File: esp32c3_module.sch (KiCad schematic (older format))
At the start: 13 parts, among them J1 Conn_01x15_Male, J2 Conn_01x15_Male, SW1 BOOT, SW2 RST, U3 ESP32-C3-MINI-1

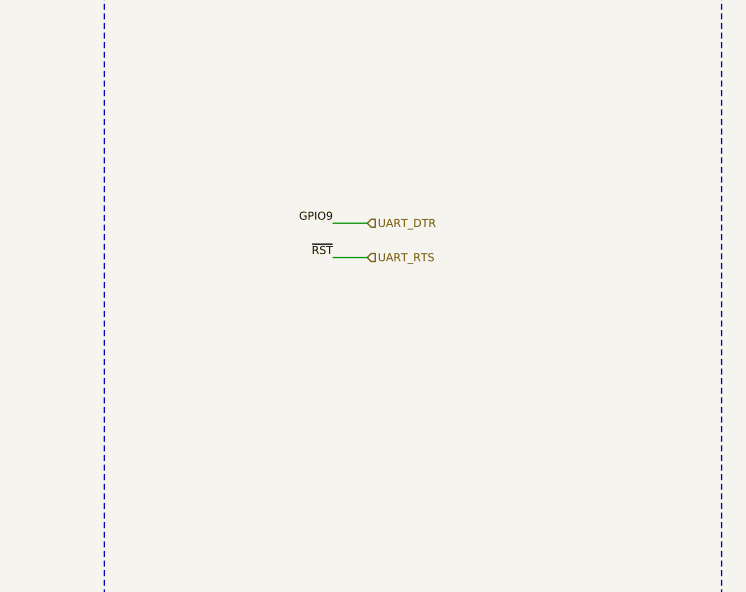
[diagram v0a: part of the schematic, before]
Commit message: Replace CP2102 with CH340X
Also add BJTs to ESP32C3 strapping pins
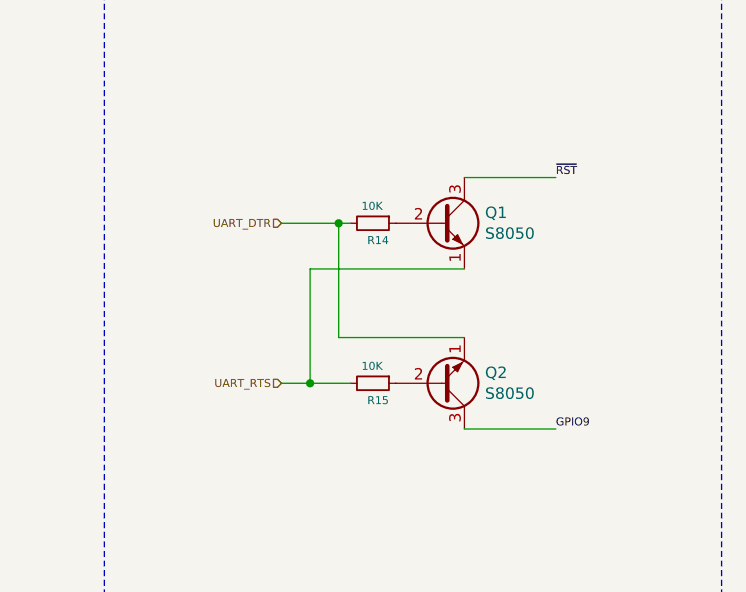
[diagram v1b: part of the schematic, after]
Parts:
- added Q1, Q2: S8050, Package_TO_SOT_SMD:SOT-23, symbol Transistor_BJT:S8050
- added R14, R15: 10K, Resistor_SMD:R_0402_1005Metric, symbol Device:R_Small
- SW1, SW2: footprint Button_Switch_SMD:SW_SPST_TL3342 -> Button_Switch_SMD:SW_SPST_CK_RS282G05A3
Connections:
- wire segments 63 -> 71
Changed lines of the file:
@@
 F 0 "SW2" H 1500 6550 35  0000 C CNN
 F 1 "RST" H 1500 6350 35  0000 C CNN
-F 2 "Button_Switch_SMD:SW_SPST_TL3342" H 1500 6600 50  0001 C CNN
+F 2 "Button_Switch_SMD:SW_SPST_CK_RS282G05A3" H 1500 6600 50  0001 C CNN
 F 3 "https://datasheet.lcsc.com/lcsc/2002271431_XKB-Connectivity-TS-1187A-B-A-B_C318884.pdf" H 1500 6600 50  0001 C CNN
 F 4 "C318884" H 1500 6400 50  0001 C CNN "LCSC"
@@
 F 0 "SW1" H 1500 6050 35  0000 C CNN
 F 1 "BOOT" H 1500 5850 35  0000 C CNN
-F 2 "Button_Switch_SMD:SW_SPST_TL3342" H 1500 6100 50  0001 C CNN
+F 2 "Button_Switch_SMD:SW_SPST_CK_RS282G05A3" H 1500 6100 50  0001 C CNN
 F 3 "https://datasheet.lcsc.com/lcsc/2002271431_XKB-Connectivity-TS-1187A-B-A-B_C318884.pdf" H 1500 6100 50  0001 C CNN
 F 4 "C318884" H 1500 5900 50  0001 C CNN "LCSC"
@@
 Text HLabel 7550 2100 0    35   Input ~ 0
 UART_RXD
-Wire Wire Line
-	9650 2300 9500 2300
-Wire Wire Line
-	9650 2450 9500 2450
-Text HLabel 9650 2300 2    35   Input ~ 0
+Text HLabel 9275 2300 0    35   Input ~ 0
 UART_DTR
-Text HLabel 9650 2450 2    35   Input ~ 0
+Text HLabel 9275 3000 0    35   Input ~ 0
 UART_RTS
 Text Label 1800 5900 0    35   ~ 0
 GPIO9
-Text Label 9500 2300 2    35   ~ 0
+Text Label 10475 3200 0    35   ~ 0
 GPIO9
 Text Label 1650 3050 2    35   ~ 0
@@
 Text Label 1150 2950 2    35   ~ 0
 GPIO8
-Text Label 9500 2450 2    35   ~ 0
+Text Label 10475 2100 0    35   ~ 0
 ~RST
 Text Label 1350 1250 2    35   ~ 0
@@
 Wire Notes Line
 	2500 4700 2500 7750
+$Comp
+L Transistor_BJT:S8050 Q1
+U 1 1 63DDD419
+P 9975 2300
+F 0 "Q1" H 10165 2346 50  0000 L CNN
+F 1 "S8050" H 10165 2255 50  0000 L CNN
+F 2 "Package_TO_SOT_SMD:SOT-23" H 10175 2225 50  0001 L CIN
+F 3 "http://www.unisonic.com.tw/datasheet/S8050.pdf" H 9975 2300 50  0001 L CNN
+F 4 "C2146" H 9975 2300 50  0001 C CNN "LCSC"
+	1    9975 2300
+	1    0    0    -1
+$EndComp
+$Comp
+L Transistor_BJT:S8050 Q2
+U 1 1 63DDD9FC
+P 9975 3000
+F 0 "Q2" H 10165 2954 50  0000 L CNN
+F 1 "S8050" H 10165 3045 50  0000 L CNN
+F 2 "Package_TO_SOT_SMD:SOT-23" H 10175 2925 50  0001 L CIN
+F 3 "http://www.unisonic.com.tw/datasheet/S8050.pdf" H 9975 3000 50  0001 L CNN
+F 4 "C2146" H 9975 3000 50  0001 C CNN "LCSC"
+	1    9975 3000
+	1    0    0    1
+$EndComp
+$Comp
+L Device:R_Small R?
+U 1 1 63DE663C
+P 9675 3000
+AR Path="/63DE663C" Ref="R?"  Part="1"
+AR Path="/63833C0B/63DE663C" Ref="R15"  Part="1"
+F 0 "R15" V 9750 2975 35  0000 L CNN
+F 1 "10K" V 9600 2950 35  0000 L CNN
+F 2 "Resistor_SMD:R_0402_1005Metric" H 9675 3000 50  0001 C CNN
+F 3 "https://datasheet.lcsc.com/lcsc/2206010100_UNI-ROYAL-Uniroyal-Elec-0402WGF1002TCE_C25744.pdf" H 9675 3000 50  0001 C CNN
+F 4 "C25744" H 9675 3000 50  0001 C CNN "LCSC"
+	1    9675 3000
+	0    1    1    0
+$EndComp
+$Comp
+L Device:R_Small R?
+U 1 1 63DE8970
+P 9675 2300
+AR Path="/63DE8970" Ref="R?"  Part="1"
+AR Path="/63833C0B/63DE8970" Ref="R14"  Part="1"
+F 0 "R14" V 9750 2275 35  0000 L CNN
+F 1 "10K" V 9600 2250 35  0000 L CNN
+F 2 "Resistor_SMD:R_0402_1005Metric" H 9675 2300 50  0001 C CNN
+F 3 "https://datasheet.lcsc.com/lcsc/2206010100_UNI-ROYAL-Uniroyal-Elec-0402WGF1002TCE_C25744.pdf" H 9675 2300 50  0001 C CNN
+F 4 "C25744" H 9675 2300 50  0001 C CNN "LCSC"
+	1    9675 2300
+	0    1    1    0
+$EndComp
+Wire Wire Line
+	9525 2300 9525 2800
+Wire Wire Line
+	9525 2800 10075 2800
+Connection ~ 9525 2300
+Wire Wire Line
+	9525 2300 9575 2300
+Wire Wire Line
+	9275 2300 9525 2300
+Wire Wire Line
+	9275 3000 9400 3000
+Wire Wire Line
+	9400 2500 9400 3000
+Wire Wire Line
+	9400 2500 10075 2500
+Connection ~ 9400 3000
+Wire Wire Line
+	9400 3000 9575 3000
+Wire Wire Line
+	10075 3200 10475 3200
+Wire Wire Line
+	10075 2100 10475 2100
 $EndSCHEMATC

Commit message: Use ESP32-C3-WROOM-02 module
Signed-off-by: Tomislav Milkovic <tomislav.milkovic95@gmail.com>
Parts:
- removed D1: USR_LED, LED_SMD:LED_0603_1608Metric, symbol Device:LED_Small
- removed R19: 470Ω, Resistor_SMD:R_0603_1608Metric, symbol Device:R_Small
- removed U3: ESP32-C3-MINI-1, Espressif:ESP32-C3-MINI-1, symbol Espressif:ESP32-C3-MINI-1
- added D1: WS2812B, LED_SMD:LED_WS2812B_PLCC4_5.0x5.0mm_P3.2mm, symbol LED:WS2812B
- added U3: ESP32-C3-WROOM-02, Espressif:ESP32-C3-WROOM-02, symbol Espressif:ESP32-C3-WROOM-02
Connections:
- net labels added: ESP32_UART_DTR, ESP32_UART_RTS, ESP32_UART_RXD, ESP32_UART_TXD, ESP32_USB_D+, ESP32_USB_D-, GPIO18, GPIO19, GPIO20, GPIO21
- net labels removed: JTAG_USB_D+, JTAG_USB_D-, UART_DTR, UART_RTS, UART_RXD, UART_TXD, USR_LED_A
- wire segments 71 -> 66
- no-connect marks 14 -> 1
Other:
- note removed: "Blue LED"
- note removed: "~~1.8 mA LED current"
- moved on the sheet: R16, R17

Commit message: Change USB UART adapter to CP2102
Signed-off-by: Tomislav Milkovic <tomislav.milkovic95@gmail.com>
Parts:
- U3: footprint Espressif:ESP32-C3-WROOM-02 -> Espressif custom:ESP32-C3-WROOM-02-SOCKET
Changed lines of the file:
@@
 $Descr A4 11693 8268
 encoding utf-8
-Sheet 4 5
+Sheet 3 5
 Title "ESP32-C3 module"
 Date "2022-11-20"
@@
 F 0 "U3" H 2725 4115 50  0000 C CNN
 F 1 "ESP32-C3-WROOM-02" H 2725 4024 50  0000 C CNN
-F 2 "Espressif:ESP32-C3-WROOM-02" H 2700 1400 50  0001 C CNN
+F 2 "Espressif custom:ESP32-C3-WROOM-02-SOCKET" H 2700 1400 50  0001 C CNN
 F 3 "https://www.espressif.com/sites/default/files/documentation/esp32-c3-wroom-02_datasheet_en.pdf" H 250 1400 50  0001 C CNN
 	1    2700 2700

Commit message: Add LCSC part numbers for all components
Signed-off-by: Tomislav Milkovic <tomislav.milkovic95@gmail.com>
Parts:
- C17: LCSC C440198 -> C19702
- D1: value WS2812B -> WS2812C; footprint LED_SMD:LED_WS2812B_PLCC4_5.0x5.0mm_P3.2mm -> LED_custom:LED_WS2812B_2.0x2.0mm_P1.13mm; LCSC (none) -> C2976072
- SW1, SW2: LCSC C318884 -> (none)
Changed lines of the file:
@@
 Sheet 3 5
 Title "ESP32-C3 module"
-Date "2022-11-20"
+Date "2025-02-16"
 Rev "1.0"
 Comp "Copyright: Tomislav Milkovic"
@@
 F 2 "Button_Switch_SMD:SW_SPST_CK_RS282G05A3" H 1500 6600 50  0001 C CNN
 F 3 "https://datasheet.lcsc.com/lcsc/2002271431_XKB-Connectivity-TS-1187A-B-A-B_C318884.pdf" H 1500 6600 50  0001 C CNN
-F 4 "C318884" H 1500 6400 50  0001 C CNN "LCSC"
+F 4 "" H 1500 6400 50  0001 C CNN "LCSC"
 	1    1500 6400
 	1    0    0    -1
@@
 F 2 "Capacitor_SMD:C_0603_1608Metric" H 1200 3850 50  0001 C CNN
 F 3 "https://datasheet.lcsc.com/lcsc/2004251506_Murata-Electronics-GRM21BR61H106KE43L_C440198.pdf" H 1200 3850 50  0001 C CNN
-F 4 "C440198" H 1200 3850 50  0001 C CNN "LCSC"
+F 4 "C19702" H 1200 3850 50  0001 C CNN "LCSC"
 	1    1200 3850
 	1    0    0    -1
@@
 F 2 "Button_Switch_SMD:SW_SPST_CK_RS282G05A3" H 1500 6100 50  0001 C CNN
 F 3 "https://datasheet.lcsc.com/lcsc/2002271431_XKB-Connectivity-TS-1187A-B-A-B_C318884.pdf" H 1500 6100 50  0001 C CNN
-F 4 "C318884" H 1500 5900 50  0001 C CNN "LCSC"
+F 4 "" H 1500 5900 50  0001 C CNN "LCSC"
 	1    1500 5900
 	1    0    0    -1
@@
 	1    0    0    -1
 $EndComp
-Text Notes 4100 7750 0    47   ~ 9
+Text Notes 4450 7750 0    47   ~ 9
 User LED
 $Comp
@@
 F 2 "Connector_PinHeader_2.54mm:PinHeader_1x15_P2.54mm_Vertical" H 7750 2600 50  0001 C CNN
 F 3 "~" H 7750 2600 50  0001 C CNN
+F 4 "" H 7750 2600 50  0001 C CNN "LCSC"
 	1    7750 2600
 	1    0    0    -1
@@
 F 2 "Connector_PinHeader_2.54mm:PinHeader_1x15_P2.54mm_Vertical" H 6200 2600 50  0001 C CNN
 F 3 "~" H 6200 2600 50  0001 C CNN
+F 4 "" H 6200 2600 50  0001 C CNN "LCSC"
 	1    6200 2600
 	1    0    0    -1
@@
 F 1 "S8050" H 10165 2255 50  0000 L CNN
 F 2 "Package_TO_SOT_SMD:SOT-23" H 10175 2225 50  0001 L CIN
-F 3 "http://www.unisonic.com.tw/datasheet/S8050.pdf" H 9975 2300 50  0001 L CNN
+F 3 "https://www.lcsc.com/datasheet/lcsc_datasheet_2310131500_Jiangsu-Changjing-Electronics-Technology-Co---Ltd--S8050-J3Y-RANGE-200-350_C2146.pdf" H 9975 2300 50  0001 L CNN
 F 4 "C2146" H 9975 2300 50  0001 C CNN "LCSC"
 	1    9975 2300
@@
 F 1 "S8050" H 10165 3045 50  0000 L CNN
 F 2 "Package_TO_SOT_SMD:SOT-23" H 10175 2925 50  0001 L CIN
-F 3 "http://www.unisonic.com.tw/datasheet/S8050.pdf" H 9975 3000 50  0001 L CNN
+F 3 "https://www.lcsc.com/datasheet/lcsc_datasheet_2310131500_Jiangsu-Changjing-Electronics-Technology-Co---Ltd--S8050-J3Y-RANGE-200-350_C2146.pdf" H 9975 3000 50  0001 L CNN
 F 4 "C2146" H 9975 3000 50  0001 C CNN "LCSC"
 	1    9975 3000
@@
 F 2 "Espressif custom:ESP32-C3-WROOM-02-SOCKET" H 2700 1400 50  0001 C CNN
 F 3 "https://www.espressif.com/sites/default/files/documentation/esp32-c3-wroom-02_datasheet_en.pdf" H 250 1400 50  0001 C CNN
+F 4 "" H 2700 2700 50  0001 C CNN "LCSC"
 	1    2700 2700
 	1    0    0    -1
@@
 U 1 1 67B7102E
 P 3525 5950
-F 0 "D1" H 3675 6200 50  0000 L CNN
-F 1 "WS2812B" H 3600 5700 50  0000 L CNN
-F 2 "LED_SMD:LED_WS2812B_PLCC4_5.0x5.0mm_P3.2mm" H 3575 5650 50  0001 L TNN
-F 3 "https://cdn-shop.adafruit.com/datasheets/WS2812B.pdf" H 3625 5575 50  0001 L TNN
+F 0 "D1" H 3650 6200 50  0000 L CNN
+F 1 "WS2812C" H 3575 5700 50  0000 L CNN
+F 2 "LED_custom:LED_WS2812B_2.0x2.0mm_P1.13mm" H 3575 5650 50  0001 L TNN
+F 3 "https://wmsc.lcsc.com/wmsc/upload/file/pdf/v2/lcsc/2202221130_Worldsemi-WS2812C-2020-V1_C2976072.pdf" H 3625 5575 50  0001 L TNN
+F 4 "C2976072" H 3525 5950 50  0001 C CNN "LCSC"
 	1    3525 5950
 	1    0    0    -1

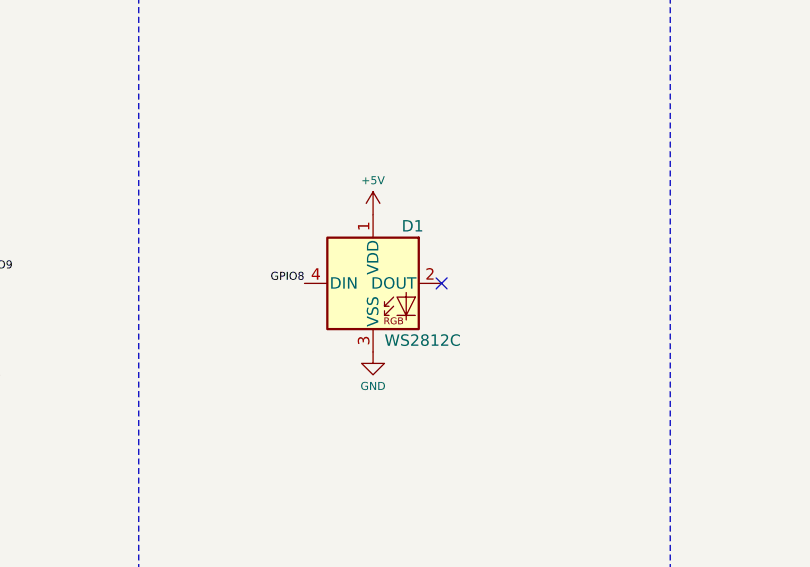
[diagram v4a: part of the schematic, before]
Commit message: Replace WS2812B with SK6805 RGB LED
Signed-off-by: Tomislav Milkovic <tomislav.milkovic95@gmail.com>
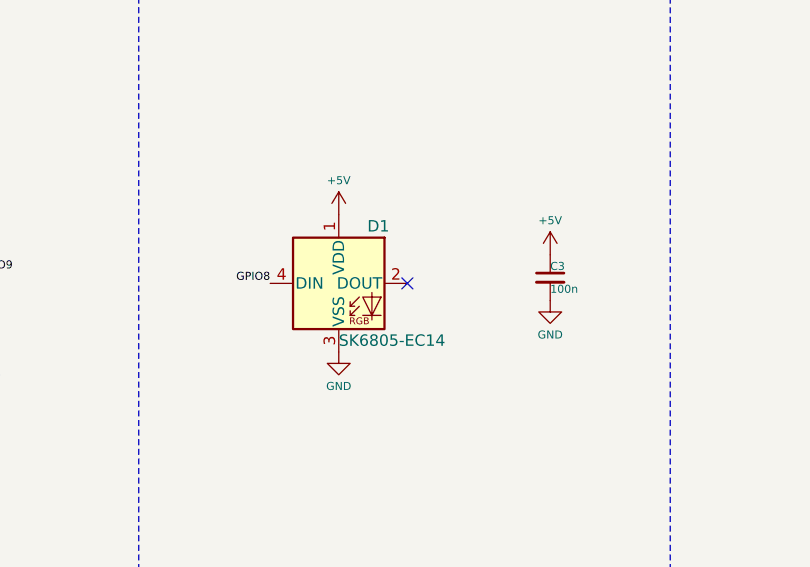
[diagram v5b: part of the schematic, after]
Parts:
- added C3: 100n, Capacitor_SMD:C_0402_1005Metric, symbol Device:C_Small
- D1: value WS2812C -> SK6805-EC14; footprint LED_custom:LED_WS2812B_2.0x2.0mm_P1.13mm -> LED_custom:LED_SK6805_E14_1.4x1.4mm_P0.4mm; LCSC C2976072 -> C2909055
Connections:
- net +5V: now also C3.1
- net GND: now also C3.2
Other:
- moved on the sheet: D1
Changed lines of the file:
@@
 L LED:WS2812B D1
 U 1 1 67B7102E
-P 3525 5950
-F 0 "D1" H 3650 6200 50  0000 L CNN
-F 1 "WS2812C" H 3575 5700 50  0000 L CNN
-F 2 "LED_custom:LED_WS2812B_2.0x2.0mm_P1.13mm" H 3575 5650 50  0001 L TNN
-F 3 "https://wmsc.lcsc.com/wmsc/upload/file/pdf/v2/lcsc/2202221130_Worldsemi-WS2812C-2020-V1_C2976072.pdf" H 3625 5575 50  0001 L TNN
-F 4 "C2976072" H 3525 5950 50  0001 C CNN "LCSC"
-	1    3525 5950
+P 3375 5950
+F 0 "D1" H 3500 6200 50  0000 L CNN
+F 1 "SK6805-EC14" H 3375 5700 50  0000 L CNN
+F 2 "LED_custom:LED_SK6805_E14_1.4x1.4mm_P0.4mm" H 3425 5650 50  0001 L TNN
+F 3 "https://wmsc.lcsc.com/wmsc/upload/file/pdf/v2/lcsc/2202161430_OPSCO-Optoelectronics-SK6805-EC14_C2909055.pdf" H 3475 5575 50  0001 L TNN
+F 4 "C2909055" H 3375 5950 50  0001 C CNN "LCSC"
+	1    3375 5950
 	1    0    0    -1
 $EndComp
@@
 L power:+5V #PWR?
 U 1 1 67B72448
-P 3525 5650
+P 3375 5650
 AR Path="/67B72448" Ref="#PWR?"  Part="1"
 AR Path="/63833C0B/67B72448" Ref="#PWR0104"  Part="1"
-F 0 "#PWR0104" H 3525 5500 50  0001 C CNN
-F 1 "+5V" H 3525 5800 35  0000 C CNN
-F 2 "" H 3525 5650 50  0001 C CNN
-F 3 "" H 3525 5650 50  0001 C CNN
-	1    3525 5650
+F 0 "#PWR0104" H 3375 5500 50  0001 C CNN
+F 1 "+5V" H 3375 5800 35  0000 C CNN
+F 2 "" H 3375 5650 50  0001 C CNN
+F 3 "" H 3375 5650 50  0001 C CNN
+	1    3375 5650
 	1    0    0    -1
 $EndComp
@@
 L power:GND #PWR?
 U 1 1 67B73827
-P 3525 6250
+P 3375 6250
 AR Path="/67B73827" Ref="#PWR?"  Part="1"
 AR Path="/63833C0B/67B73827" Ref="#PWR0105"  Part="1"
-F 0 "#PWR0105" H 3525 6000 50  0001 C CNN
-F 1 "GND" H 3525 6100 35  0000 C CNN
-F 2 "" H 3525 6250 50  0001 C CNN
-F 3 "" H 3525 6250 50  0001 C CNN
-	1    3525 6250
+F 0 "#PWR0105" H 3375 6000 50  0001 C CNN
+F 1 "GND" H 3375 6100 35  0000 C CNN
+F 2 "" H 3375 6250 50  0001 C CNN
+F 3 "" H 3375 6250 50  0001 C CNN
+	1    3375 6250
 	1    0    0    -1
 $EndComp
-Text Label 3225 5950 2    35   ~ 0
+Text Label 3075 5950 2    35   ~ 0
 GPIO8
-NoConn ~ 3825 5950
+NoConn ~ 3675 5950
 Wire Wire Line
 	6000 2300 5450 2300
@@
 Wire Notes Line
 	500  7750 4825 7750
+$Comp
+L Device:C_Small C?
+U 1 1 67B47D6D
+P 4300 5925
+AR Path="/67B47D6D" Ref="C?"  Part="1"
+AR Path="/63833C0B/67B47D6D" Ref="C3"  Part="1"
+F 0 "C3" H 4300 5975 35  0000 L CNN
+F 1 "100n" H 4300 5875 35  0000 L CNN
+F 2 "Capacitor_SMD:C_0402_1005Metric" H 4300 5925 50  0001 C CNN
+F 3 "https://datasheet.lcsc.com/lcsc/1810191222_Samsung-Electro-Mechanics-CL05B104KB54PNC_C307331.pdf" H 4300 5925 50  0001 C CNN
+F 4 "C307331" H 4300 5925 50  0001 C CNN "LCSC"
+	1    4300 5925
+	1    0    0    -1
+$EndComp
+$Comp
+L power:+5V #PWR?
+U 1 1 67B4AE7F
+P 4300 5825
+AR Path="/67B4AE7F" Ref="#PWR?"  Part="1"
+AR Path="/63833C0B/67B4AE7F" Ref="#PWR050"  Part="1"
+F 0 "#PWR050" H 4300 5675 50  0001 C CNN
+F 1 "+5V" H 4300 5975 35  0000 C CNN
+F 2 "" H 4300 5825 50  0001 C CNN
+F 3 "" H 4300 5825 50  0001 C CNN
+	1    4300 5825
+	1    0    0    -1
+$EndComp
+$Comp
+L power:GND #PWR?
+U 1 1 67B4B1E3
+P 4300 6025
+AR Path="/67B4B1E3" Ref="#PWR?"  Part="1"
+AR Path="/63833C0B/67B4B1E3" Ref="#PWR051"  Part="1"
+F 0 "#PWR051" H 4300 5775 50  0001 C CNN
+F 1 "GND" H 4300 5875 35  0000 C CNN
+F 2 "" H 4300 6025 50  0001 C CNN
+F 3 "" H 4300 6025 50  0001 C CNN
+	1    4300 6025
+	1    0    0    -1
+$EndComp
 $EndSCHEMATC
